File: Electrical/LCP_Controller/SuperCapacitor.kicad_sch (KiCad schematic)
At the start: 27 parts, among them Q3 FDN537N, U4 LTC3225, U5 ADM4210

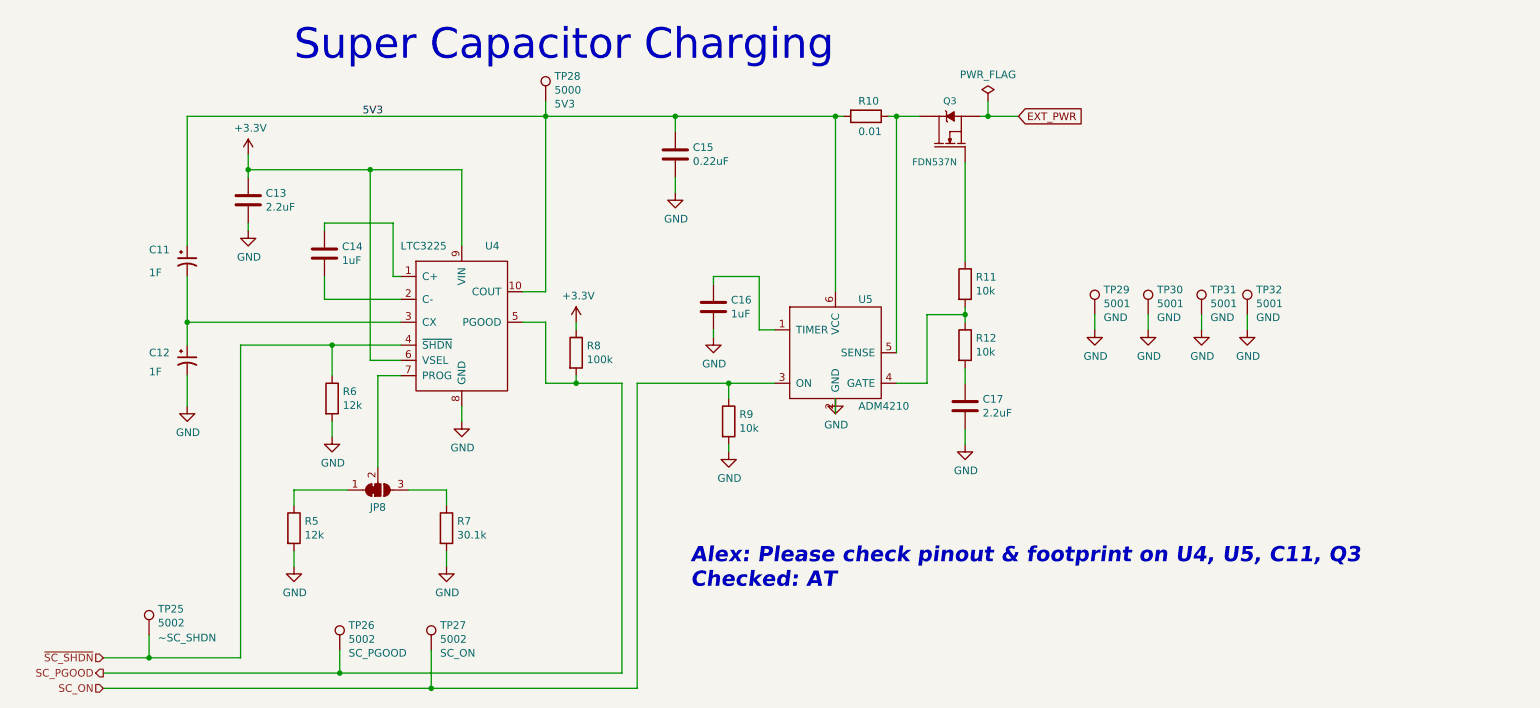
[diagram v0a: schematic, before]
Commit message: Hardware Revision : v0.3
1. modified schematic design, removed unnecessary test points.
2. pcb layout 2x8 Inches allowance dimension, layout is in progress
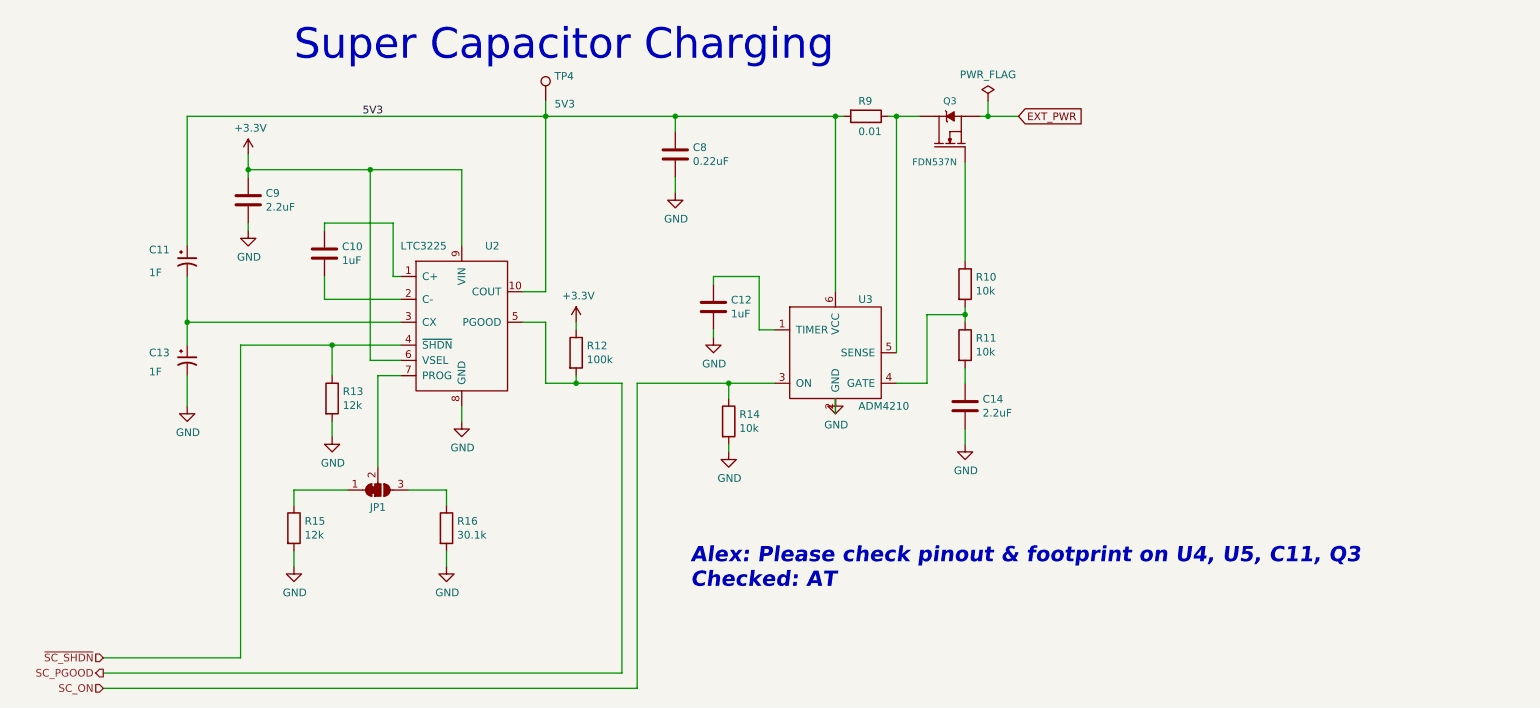
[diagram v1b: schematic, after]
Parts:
- removed TP25, TP26, TP27: 5002, TestPoint:TestPoint_Keystone_5000-5004_Miniature, symbol Connector:TestPoint
- removed TP29, TP30, TP31, TP32: 5001, TestPoint:TestPoint_Keystone_5000-5004_Miniature, symbol Connector:TestPoint
- renumbered C14 to C10, C16 to C12, C12 to C13, C17 to C14, C15 to C8, C13 to C9, JP8 to JP1, R11 to R10, R12 to R11, R8 to R12, R6 to R13, R9 to R14, R5 to R15, R7 to R16, R10 to R9, TP28 to TP4, U4 to U2, U5 to U3

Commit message: PCB layout : update , WIP
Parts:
- TP4: value 5000 -> 5V3
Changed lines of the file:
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@@
       (effects (font (size 1.27 1.27)) (justify left))
     )
-    (property "Value" "5000" (id 1) (at 139.9032 68.0212 0)
+    (property "Value" "5V3" (id 1) (at 139.9032 68.0212 0)
       (effects (font (size 1.27 1.27)) (justify left) hide)
     )

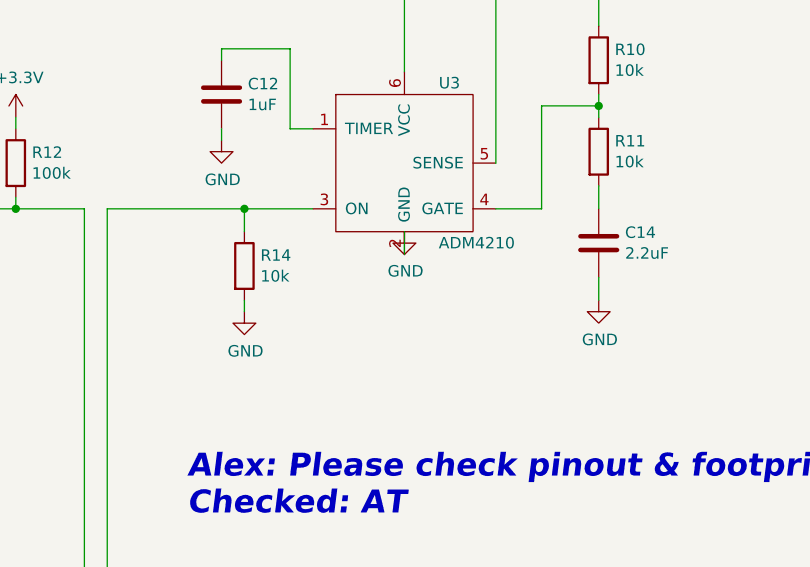
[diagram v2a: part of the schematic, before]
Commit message: Hw Rev : 0.3v
changed buck-coverter LMR50410XDBVR to BD9G102G-LB, added schotty diode.
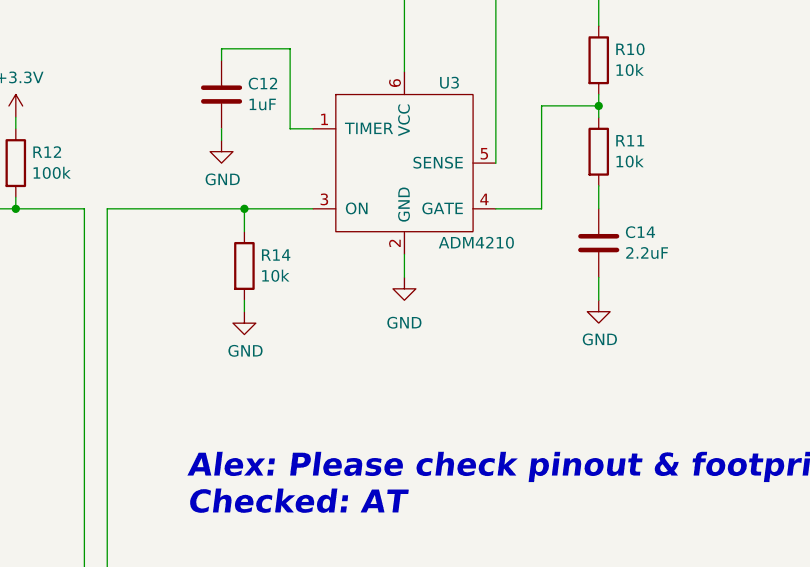
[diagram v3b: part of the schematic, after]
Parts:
- C11, C13: MPN (none) -> HV0810-2R7105-R
- C14, C9: MPN CL21B225KOFNFNE -> CL21A225KB9LNNC
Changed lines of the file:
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@@
-    (stroke (width 0) (type default) (color 0 0 0 0))
-  )
-  (wire (pts (xy 186.69 119.38) (xy 186.69 121.92))
     (stroke (width 0) (type default) (color 0 0 0 0))
   )
@@
   )
   (wire (pts (xy 87.63 162.56) (xy 87.63 110.49))
+    (stroke (width 0) (type default) (color 0 0 0 0))
+  )
+  (wire (pts (xy 186.69 121.92) (xy 186.69 124.46))
     (stroke (width 0) (type default) (color 0 0 0 0))
   )
@@
       (effects (font (size 1.27 1.27)) hide)
     )
-    (property "MPN" "CL21B225KOFNFNE" (id 4) (at 88.9 86.36 0)
+    (property "MPN" "CL21A225KB9LNNC" (id 4) (at 88.9 86.36 0)
       (effects (font (size 1.27 1.27)) hide)
     )
@@
     (pin "1")
   )
-  (symbol (lib_id "power:GND") (at 186.69 119.38 0) (unit 1)
-    (in_bom yes) (on_board yes)
-    (property "Reference" "#PWR020" (id 0) (at 186.69 125.73 0)
-      (effects (font (size 1.27 1.27)) hide)
-    )
-    (property "Value" "GND" (id 1) (at 186.817 123.7742 0))
-    (property "Footprint" "" (id 2) (at 186.69 119.38 0)
-      (effects (font (size 1.27 1.27)) hide)
-    )
-    (property "Datasheet" "" (id 3) (at 186.69 119.38 0)
-      (effects (font (size 1.27 1.27)) hide)
-    )
-    (pin "1")
-  )
   (symbol (lib_id "Device:C") (at 160.02 78.74 0) (unit 1)
     (in_bom yes) (on_board yes)
@@
       (effects (font (size 1.27 1.27)) hide)
     )
-    (property "MPN" "CL21B225KOFNFNE" (id 4) (at 208.28 120.65 0)
+    (property "MPN" "CL21A225KB9LNNC" (id 4) (at 208.28 120.65 0)
       (effects (font (size 1.27 1.27)) hide)
     )
@@
     (pin "1")
   )
+  (symbol (lib_id "power:GND") (at 186.69 124.46 0) (unit 1)
+    (in_bom yes) (on_board yes) (fields_autoplaced)
+    (property "Reference" "#PWR0110" (id 0) (at 186.69 130.81 0)
+      (effects (font (size 1.27 1.27)) hide)
+    )
+    (property "Value" "GND" (id 1) (at 186.69 129.54 0))
+    (property "Footprint" "" (id 2) (at 186.69 124.46 0)
+      (effects (font (size 1.27 1.27)) hide)
+    )
+    (property "Datasheet" "" (id 3) (at 186.69 124.46 0)
+      (effects (font (size 1.27 1.27)) hide)
+    )
+    (pin "1")
+  )
   (symbol (lib_id "Device:C_Polarized_Small_US") (at 78.74 113.03 0) (unit 1)
     (in_bom yes) (on_board yes)
@@
       (effects (font (size 1.27 1.27)) hide)
     )
+    (property "MPN" "HV0810-2R7105-R" (id 5) (at 78.74 113.03 0)
+      (effects (font (size 1.27 1.27)) hide)
+    )
     (pin "1")
     (pin "2")
@@
       (effects (font (size 1.27 1.27)) hide)
     )
+    (property "MPN" "HV0810-2R7105-R" (id 4) (at 78.74 96.52 0)
+      (effects (font (size 1.27 1.27)) hide)
+    )

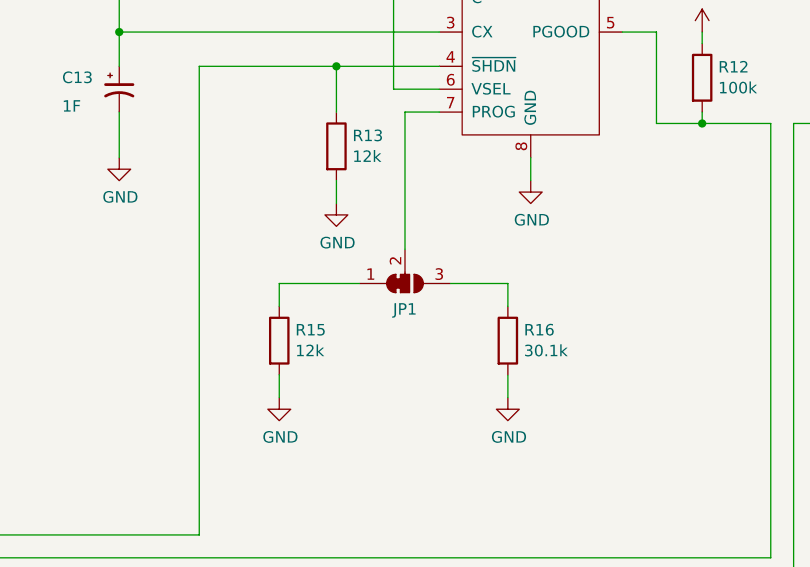
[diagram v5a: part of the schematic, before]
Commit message: Removed RF Switch
Deleted the RF Switch.

GPS Signal is routed to J17 and Iridium to J18.
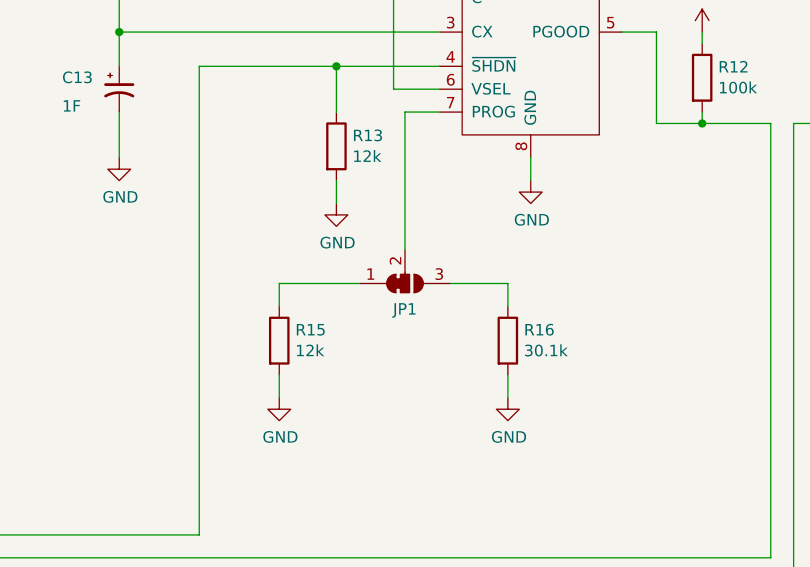
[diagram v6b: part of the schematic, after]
